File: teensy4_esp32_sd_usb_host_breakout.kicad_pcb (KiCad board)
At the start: 2 copper layers, 22.9 x 55.9 mm, 36 parts, among them J1 Conn_01x14, J2 USB_A, J3 Conn_01x14, J4 Micro_SD_Card_Det_Hirose_DM3AT, J5 Conn_01x08, J6 Conn_01x04, J7 Conn_01x01, SW2 PROGRAM, U1 TPD3S014, U2 TLV75733PDBVR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

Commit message: Second draft
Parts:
- JP1: footprint Jumper:SolderJumper-2_P1.3mm_Bridged_RoundedPad1.0x1.5mm -> Jumper:SolderJumper-2_P1.3mm_Open_RoundedPad1.0x1.5mm

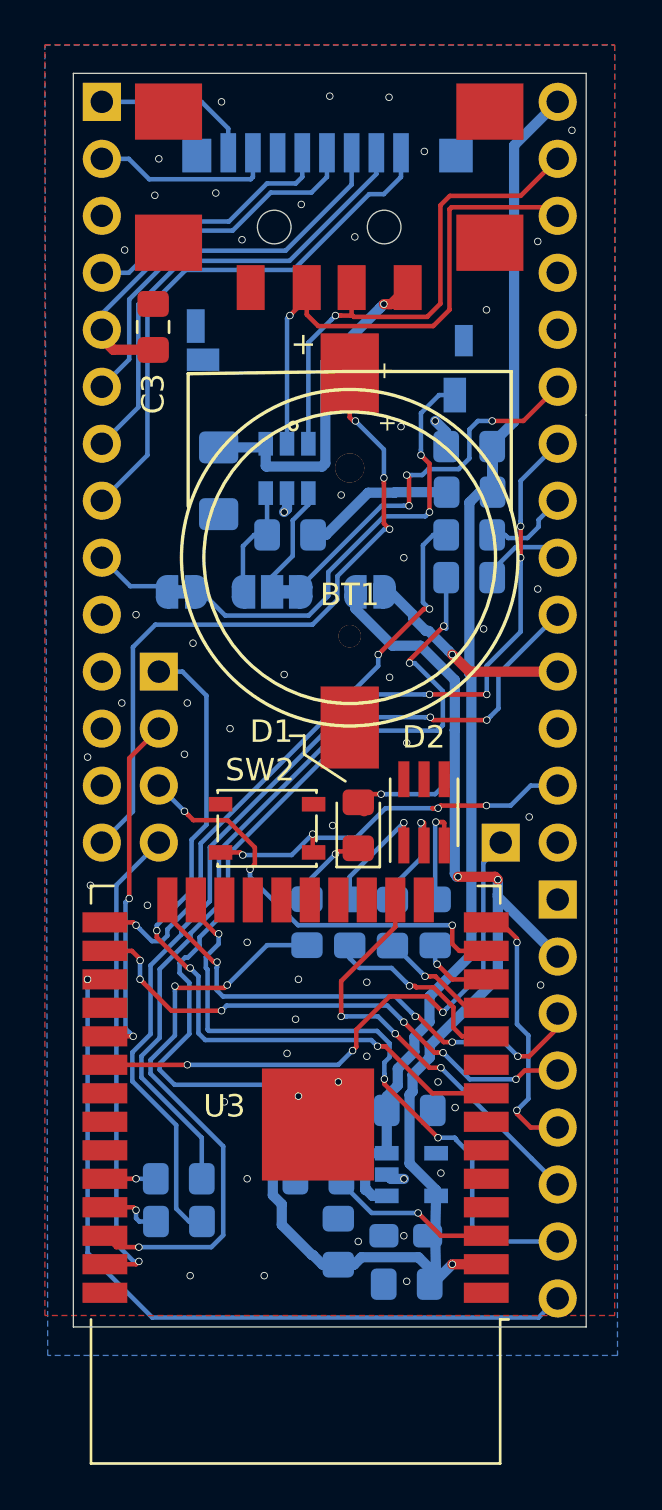
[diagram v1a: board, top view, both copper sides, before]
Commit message: Update readme, fix via sizes
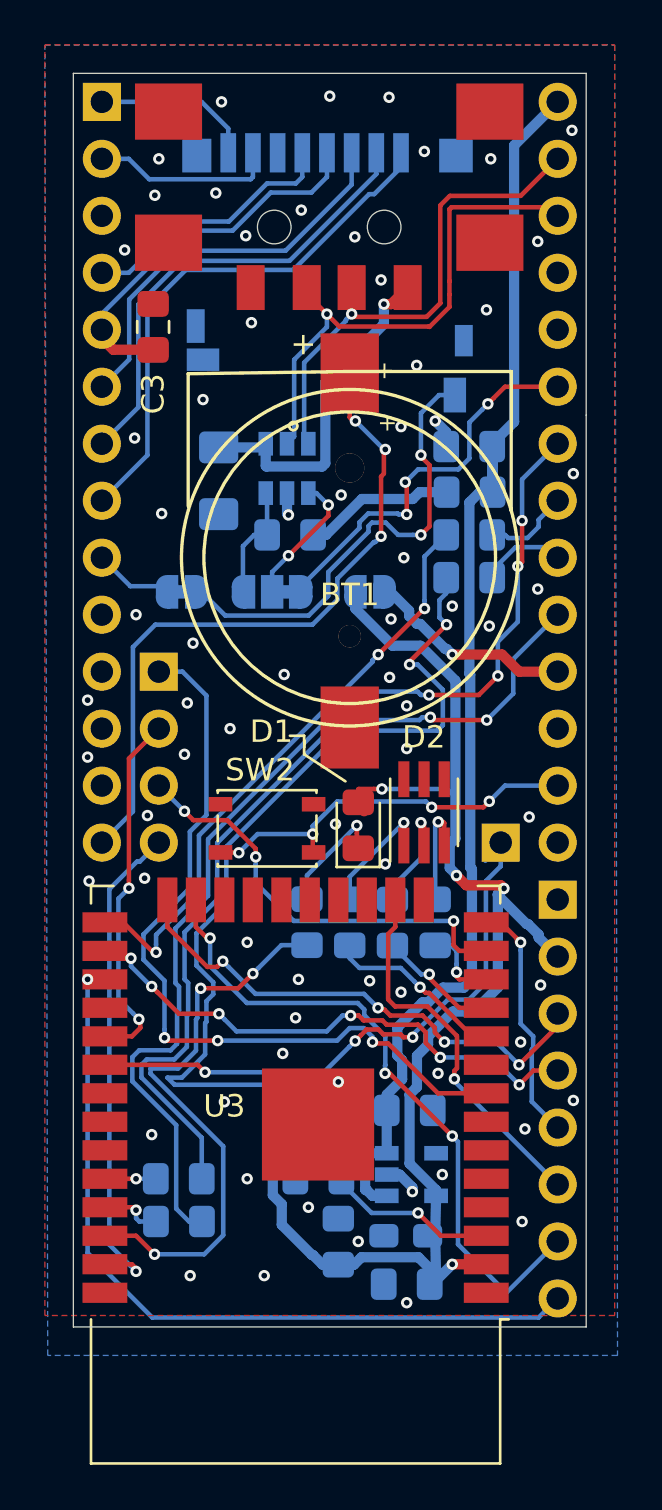
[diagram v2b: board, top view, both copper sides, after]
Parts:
- C3: value 0.1u -> 10u
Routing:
- net /IO13: track 18.9 -> 16.9 mm, vias 3 -> 1
- net /IO32_ESP_BUSY: track 34.3 -> 36.3 mm
- net Net-(D1-Pad1): track 3.60 -> 5.38 mm
- net /D+: track 24.9 -> 23.5 mm
- net /IO4: track 23.4 -> 24.7 mm
- net /25: track 47.4 -> 48.5 mm
- net +3V3: track 63.4 -> 64.5 mm
- net /24: track 37.6 -> 38.7 mm
- net /IO26_GREEN: track 5.33 -> 6.37 mm
- net /IO18_SCK: track 25.7 -> 26.7 mm
- net /SD_DET: track 19.9 -> 20.9 mm
- net /EN: track 4.82 -> 5.77 mm, vias 0 -> 2
- net /IO12: track 12.0 -> 11.1 mm, vias 2 -> 1
- net /VUSB: track 56.0 -> 56.9 mm
- net /IO15: track 29.3 -> 30.2 mm
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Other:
- net class Default: via_dia 0.3302 -> 0.508
- rule via_min_size: 0.3302 -> 0.508

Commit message: Version 1.0 Ordered
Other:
- rule pad_to_mask_clearance: 0.051 -> 0.0508
- rule solder_mask_min_width: 0.25 -> 0.1016
- board text added: "IO16 IO15 IO13 IO12 IO4 IO2 3v3 GND"
- board text added: "Teensy 4.0 USB/SD/ESP32 Breakout v1.0"
- board text removed: "Teensy 4.0 USB/SD/ESP32 Breakout 2020-03-08"
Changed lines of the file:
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@@
   (general
     (thickness 1.6)
-    (drawings 12)
+    (drawings 23)
     (tracks 790)
     (zones 0)
@@
     (via_min_drill 0.254)
     (user_via 0.508 0.254)
-    (uvia_size 0.3)
-    (uvia_drill 0.1)
+    (uvia_size 0.508)
+    (uvia_drill 0.254)
     (uvias_allowed no)
-    (uvia_min_size 0.2)
-    (uvia_min_drill 0.1)
+    (uvia_min_size 0.508)
+    (uvia_min_drill 0.254)
     (edge_width 0.05)
     (segment_width 0.2)
@@
     (pad_size 1.7 1.7)
     (pad_drill 1)
-    (pad_to_mask_clearance 0.051)
-    (solder_mask_min_width 0.25)
+    (pad_to_mask_clearance 0.0508)
+    (solder_mask_min_width 0.1016)
     (aux_axis_origin 0 0)
     (visible_elements FFFFFF7F)
@@
     (via_dia 0.508)
     (via_drill 0.254)
-    (uvia_dia 0.3)
-    (uvia_drill 0.1)
+    (uvia_dia 0.508)
+    (uvia_drill 0.254)
     (add_net +3V3)
     (add_net /24)
@@
     (tags "resistor handsolder")
     (attr smd)
-    (fp_text reference R8 (at 2.658 0) (layer B.SilkS)
+    (fp_text reference R8 (at 2.658 -0.254) (layer B.SilkS)
       (effects (font (size 1 1) (thickness 0.15)) (justify mirror))
     )
@@
     (tags "resistor handsolder")
     (attr smd)
-    (fp_text reference R7 (at 2.667 0.762) (layer B.SilkS)
+    (fp_text reference R7 (at 2.667 0.381) (layer B.SilkS)
       (effects (font (size 1 1) (thickness 0.15)) (justify mirror))
     )
@@
     (tags "resistor handsolder")
     (attr smd)
-    (fp_text reference R4 (at 0 1.65 90) (layer B.SilkS)
+    (fp_text reference R4 (at -2.676 -0.762 180) (layer B.SilkS)
       (effects (font (size 1 1) (thickness 0.15)) (justify mirror))
     )
@@
     )
   )
+  (gr_text "IO16  IO15  IO13  IO12  IO4    IO2  3v3    GND" (at 150.876 143.383 90) (layer F.SilkS)
+    (effects (font (size 0.508 0.508) (thickness 0.127)))
+  )
+  (gr_line (start 148.59 133.35) (end 151.13 133.35) (layer F.SilkS) (width 0.12))
+  (gr_line (start 148.59 130.81) (end 148.59 133.35) (layer F.SilkS) (width 0.12))
+  (gr_line (start 151.13 130.81) (end 148.59 130.81) (layer F.SilkS) (width 0.12))
+  (gr_line (start 135.89 123.19) (end 133.35 123.19) (layer F.SilkS) (width 0.12))
+  (gr_line (start 135.89 133.35) (end 135.89 123.19) (layer F.SilkS) (width 0.12))
+  (gr_line (start 130.81 133.35) (end 135.89 133.35) (layer F.SilkS) (width 0.12))
+  (gr_line (start 133.35 97.79) (end 133.35 133.35) (layer F.SilkS) (width 0.12))
+  (gr_line (start 151.13 133.35) (end 151.13 97.79) (layer F.SilkS) (width 0.12))
+  (gr_line (start 153.67 133.35) (end 151.13 133.35) (layer F.SilkS) (width 0.12))
+  (gr_line (start 151.13 133.35) (end 153.67 133.35) (layer F.SilkS) (width 0.12))
   (gr_line (start 141.097 127.3175) (end 140.462 127.3175) (layer F.SilkS) (width 0.12))
   (gr_line (start 141.097 128.143) (end 141.097 127.3175) (layer F.SilkS) (width 0.12))
@@
   (gr_line (start 153.67 97.79) (end 153.67 113.03) (layer Edge.Cuts) (width 0.05))
   (gr_line (start 130.81 97.79) (end 153.67 97.79) (layer Edge.Cuts) (width 0.05))
-  (gr_text "Teensy 4.0 \nUSB/SD/ESP32\nBreakout\n2020-03-08" (at 142.24 129.413) (layer B.SilkS)
+  (gr_text "Teensy 4.0 \nUSB/SD/ESP32\nBreakout v1.0" (at 142.24 129.413) (layer B.SilkS)
     (effects (font (size 0.889 0.889) (thickness 0.127)) (justify mirror))
   )
